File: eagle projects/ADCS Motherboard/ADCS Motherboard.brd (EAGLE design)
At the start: 91 x 91 mm, 142 parts, among them J1 HDR_10_EZFET_DEBUGGER, J11 CNC_3221-10-0300-00, J5 CNC_3221-10-0300-00, J7 TE-1734829-3, Q1 BSR802NL6327HTSA1, Q2 IRLML6246TRPBF, Q3 IRLML2246TRPBF, U1 MSP430F5529IPN, U10 TSV991AILT, U2 TSV991AILT, U3 ADS7841E_2K5, U4 TSV991AILT, U7 HMC1053, U9 BMX160, Y1 32.768kHz, Y2 CSTCR4M00G15L99, Y3 32.768kHz

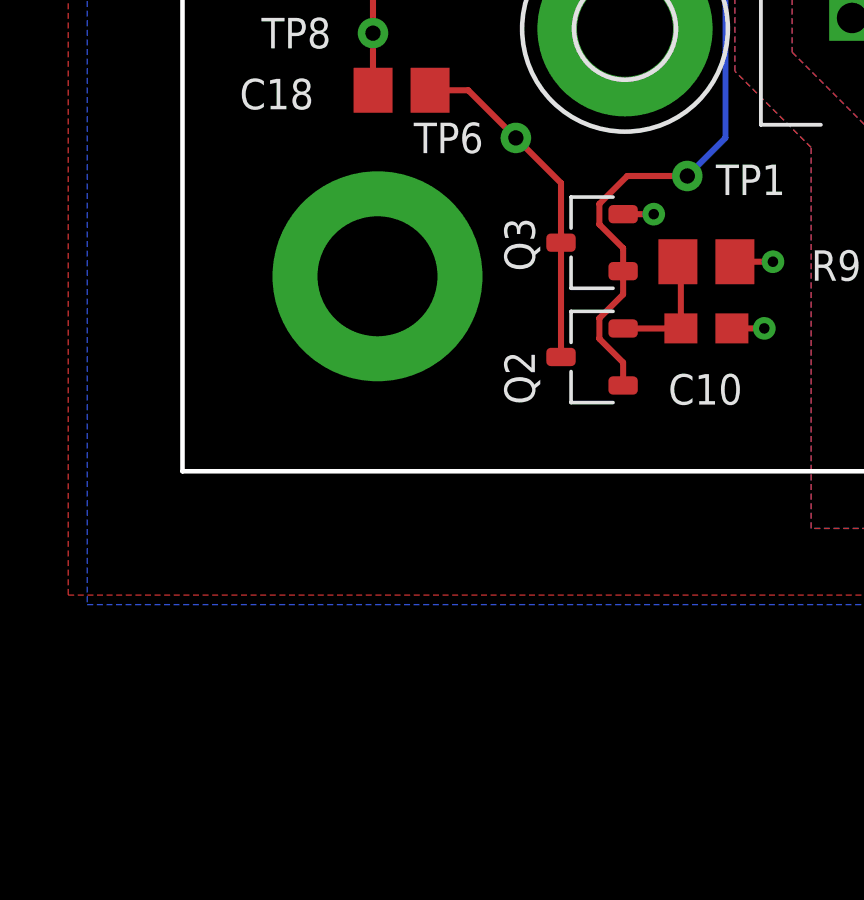
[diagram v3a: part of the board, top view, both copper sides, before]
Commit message: Replace totem pole driver with complementary Mosfets pair package
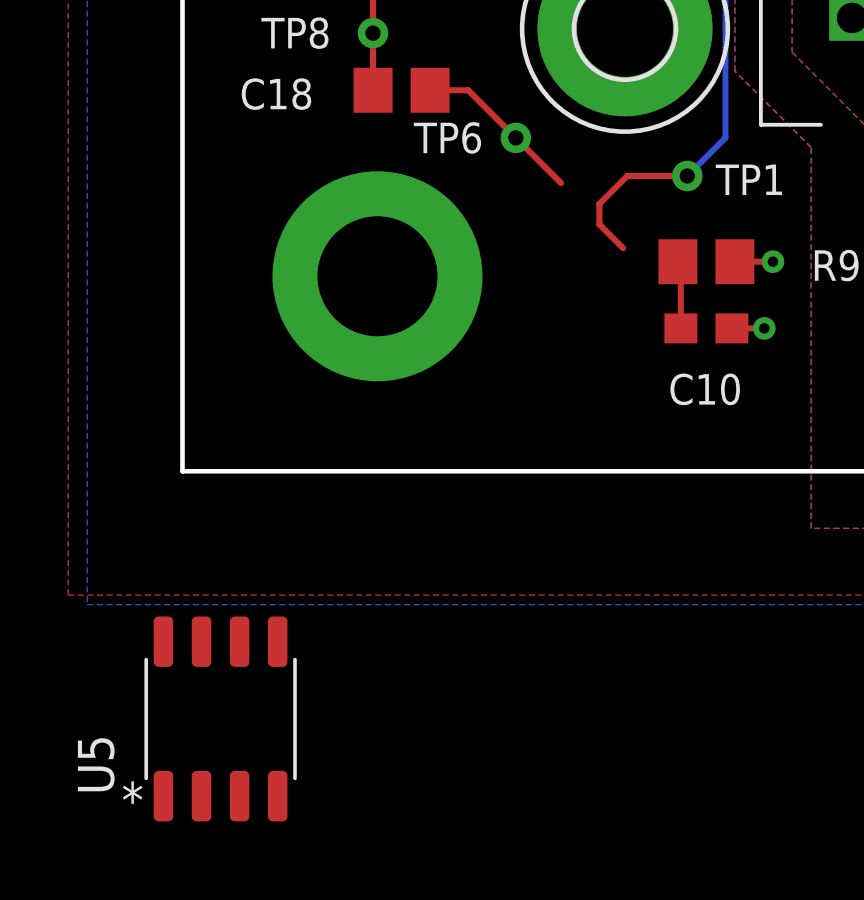
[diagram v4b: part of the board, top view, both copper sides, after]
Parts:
- removed Q2: IRLML6246TRPBF, my_library:SOT23-3P95_237X112L25X40N_MICRO3
- removed Q3: IRLML2246TRPBF, my_library:SOT23-3P95_237X112L25X40N_MICRO3
- added U5: DMC4050SSDQ-13, my_library:SOIC8P127_490X600X175L72X40N_DMC4050SSDQ-13
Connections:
- net GND: now also U5.3; no longer Q3.2
- net HMC1053_RESET: now also U5.2, U5.4; no longer Q2.1, Q3.1
- net N$39: now also U5.1; no longer Q2.2
- net N$9: now also U5.6, U5.7; no longer Q2.3, Q3.3
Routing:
- net N$9: track 11.4 -> 5.65 mm
- net HMC1053_RESET: track 106.7 -> 101.5 mm
- net N$39: track 4.19 -> 2.27 mm
- net GND: track 72.0 -> 71.0 mm, vias 96 -> 95
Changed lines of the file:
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@@
 <attribute name="NAME" x="71.12" y="48.895" size="1.016" layer="25" ratio="10" rot="R180"/>
-</element>
-<element name="Q3" library="my_library" library_urn="urn:adsk.eagle:library:22876504" package="SOT23-3P95_237X112L25X40N_MICRO3" package3d_urn="urn:adsk.eagle:package:24628516/1" value="IRLML2246TRPBF" x="13.6525" y="7.62" smashed="yes" rot="R90">
-<attribute name="NAME" x="11.7475" y="6.6675" size="1.016" layer="25" ratio="10" rot="R90"/>
-</element>
-<element name="Q2" library="my_library" library_urn="urn:adsk.eagle:library:22876504" package="SOT23-3P95_237X112L25X40N_MICRO3" package3d_urn="urn:adsk.eagle:package:24628516/1" value="IRLML6246TRPBF" x="13.6525" y="3.81" smashed="yes" rot="R90">
-<attribute name="NAME" x="11.7475" y="2.2225" size="1.016" layer="25" ratio="10" rot="R90"/>
 </element>
 <element name="J4" library="my_library" library_urn="urn:adsk.eagle:library:22876504" package="1X02" package3d_urn="urn:adsk.eagle:package:24527019/1" value="" x="15.875" y="62.23" smashed="yes">
@@
 <attribute name="POPULARITY" value="35" x="84.455" y="68.2625" size="1.778" layer="27" rot="R90" display="off"/>
 <attribute name="VALUE" x="88.9" y="61.9125" size="1.27" layer="27" rot="R90"/>
+</element>
+<element name="U5" library="my_library" library_urn="urn:adsk.eagle:library:22876504" package="SOIC8P127_490X600X175L72X40N_DMC4050SSDQ-13" value="DMC4050SSDQ-13" x="1.27" y="-8.255" smashed="yes">
+<attribute name="NAME" x="-2.286" y="-10.795" size="1.2" layer="25" font="vector" ratio="10" rot="R90"/>
 </element>
 </elements>
@@
 <contactref element="R36" pad="1"/>
 <contactref element="Q1" pad="2"/>
-<contactref element="Q3" pad="2"/>
-<wire x1="14.6875" y1="8.57" x2="15.7081" y2="8.57" width="0.2032" layer="1"/>
-<via x="15.7081" y="8.57" extent="1-16" drill="0.35"/>
 <wire x1="66.0631" y1="23.226" x2="66.0146" y2="23.1775" width="0.2032" layer="1"/>
 <wire x1="72.175" y1="51.7525" x2="71.0944" y2="51.7525" width="0.2032" layer="1"/>
@@
 <wire x1="83.955" y1="36.195" x2="83.0744" y2="36.195" width="0.2032" layer="1"/>
 <via x="83.0744" y="36.195" extent="1-16" drill="0.35"/>
+<contactref element="U5" pad="3"/>
 <wire x1="66.0631" y1="24.1681" x2="66.03960625" y2="24.130009375" width="0" layer="19" extent="1-1"/>
+<wire x1="1.905" y1="-10.83" x2="18.3125" y2="4.7625" width="0" layer="19" extent="1-1"/>
 </signal>
 <signal name="TARGET_PUR">
@@
 <signal name="HMC1053_RESET">
 <contactref element="TP1" pad="1"/>
-<contactref element="Q3" pad="1"/>
-<contactref element="Q2" pad="1"/>
 <via x="34.925" y="49.53" extent="1-16" drill="0.35"/>
 <wire x1="13.8959" y1="8.91238125" x2="13.8959" y2="8.22761875" width="0.2032" layer="1"/>
@@
 <wire x1="14.82601875" y1="9.8425" x2="13.8959" y2="8.91238125" width="0.2032" layer="1"/>
 <wire x1="13.8959" y1="8.22761875" x2="14.6875" y2="7.43601875" width="0.2032" layer="1"/>
-<wire x1="14.6875" y1="7.43601875" x2="14.6875" y2="6.67" width="0.2032" layer="1"/>
 <contactref element="U1" pad="2"/>
 <wire x1="68.023025" y1="49.8602" x2="38.19795" y2="49.8602" width="0.2032" layer="1"/>
@@
 <wire x1="29.5275" y1="46.6725" x2="32.0675" y2="46.6725" width="0.2032" layer="16"/>
 <wire x1="32.0675" y1="46.6725" x2="34.925" y2="49.53" width="0.2032" layer="16"/>
-<wire x1="13.8959" y1="5.10238125" x2="13.8959" y2="4.41761875" width="0.2032" layer="1"/>
-<wire x1="14.6875" y1="6.67" x2="14.6875" y2="5.89398125" width="0.2032" layer="1"/>
-<wire x1="14.6875" y1="3.62601875" x2="14.6875" y2="2.86" width="0.2032" layer="1"/>
-<wire x1="14.6875" y1="5.89398125" x2="13.8959" y2="5.10238125" width="0.2032" layer="1"/>
-<wire x1="13.8959" y1="4.41761875" x2="14.6875" y2="3.62601875" width="0.2032" layer="1"/>
 <wire x1="18.0975" y1="36.5125" x2="18.0975" y2="11.1125" width="0.2032" layer="16"/>
 <wire x1="18.0975" y1="11.1125" x2="16.8275" y2="9.8425" width="0.2032" layer="16"/>
@@
 <wire x1="71.56" y1="41.308025" x2="69.644" y2="43.224025" width="0.2032" layer="1"/>
 <wire x1="69.644" y1="48.239225" x2="68.023025" y2="49.8602" width="0.2032" layer="1"/>
+<contactref element="U5" pad="4"/>
+<contactref element="U5" pad="2"/>
+<wire x1="3.175" y1="-10.83" x2="14.6875" y2="7.43601875" width="0" layer="19" extent="1-1"/>
+<wire x1="0.635" y1="-10.83" x2="3.175" y2="-10.83" width="0" layer="19" extent="1-1"/>
 </signal>
 <signal name="N$39">
 <contactref element="C10" pad="2"/>
 <contactref element="R9" pad="1"/>
-<contactref element="Q2" pad="2"/>
 <wire x1="16.6125" y1="4.7625" x2="16.61" y2="4.76" width="0.2032" layer="1"/>
-<wire x1="16.61" y1="4.76" x2="14.6875" y2="4.76" width="0.2032" layer="1"/>
 <wire x1="16.5125" y1="6.985" x2="16.6125" y2="6.885" width="0.2032" layer="1"/>
 <wire x1="16.6125" y1="6.885" x2="16.6125" y2="4.7625" width="0.2032" layer="1"/>
+<contactref element="U5" pad="1"/>
+<wire x1="-0.635" y1="-10.83" x2="16.6125" y2="4.7625" width="0" layer="19" extent="1-1"/>
 </signal>
 <signal name="OUT_B_P" class="1">
@@
 <signal name="N$9">
 <contactref element="C18" pad="1"/>
-<wire x1="12.6175" y1="3.81" x2="12.6175" y2="7.62" width="0.2032" layer="1"/>
-<contactref element="Q3" pad="3"/>
-<contactref element="Q2" pad="3"/>
 <contactref element="TP6" pad="1"/>
 <wire x1="8.2525" y1="12.7" x2="9.525" y2="12.7" width="0.2032" layer="1"/>
 <wire x1="11.1125" y1="11.1125" x2="9.525" y2="12.7" width="0.2032" layer="1"/>
 <wire x1="11.1125" y1="11.1125" x2="12.6175" y2="9.6075" width="0.2032" layer="1"/>
-<wire x1="12.6175" y1="9.6075" x2="12.6175" y2="7.62" width="0.2032" layer="1"/>
+<contactref element="U5" pad="7"/>
+<contactref element="U5" pad="6"/>
+<wire x1="1.905" y1="-5.68" x2="12.6175" y2="9.6075" width="0" layer="19" extent="1-1"/>
+<wire x1="0.635" y1="-5.68" x2="1.905" y2="-5.68" width="0" layer="19" extent="1-1"/>
 </signal>
 <signal name="UCB1_I2C_SCL">

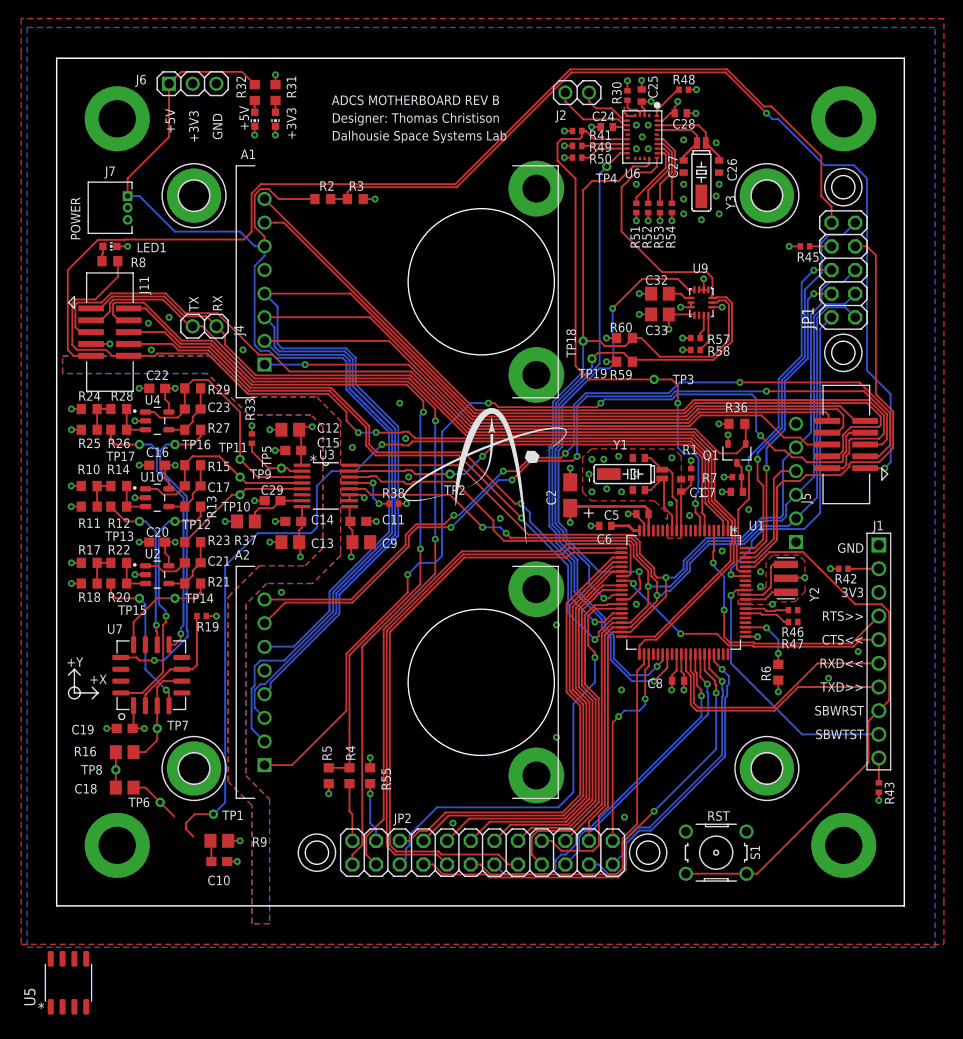
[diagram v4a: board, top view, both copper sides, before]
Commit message: Added new mosfet pair to layout
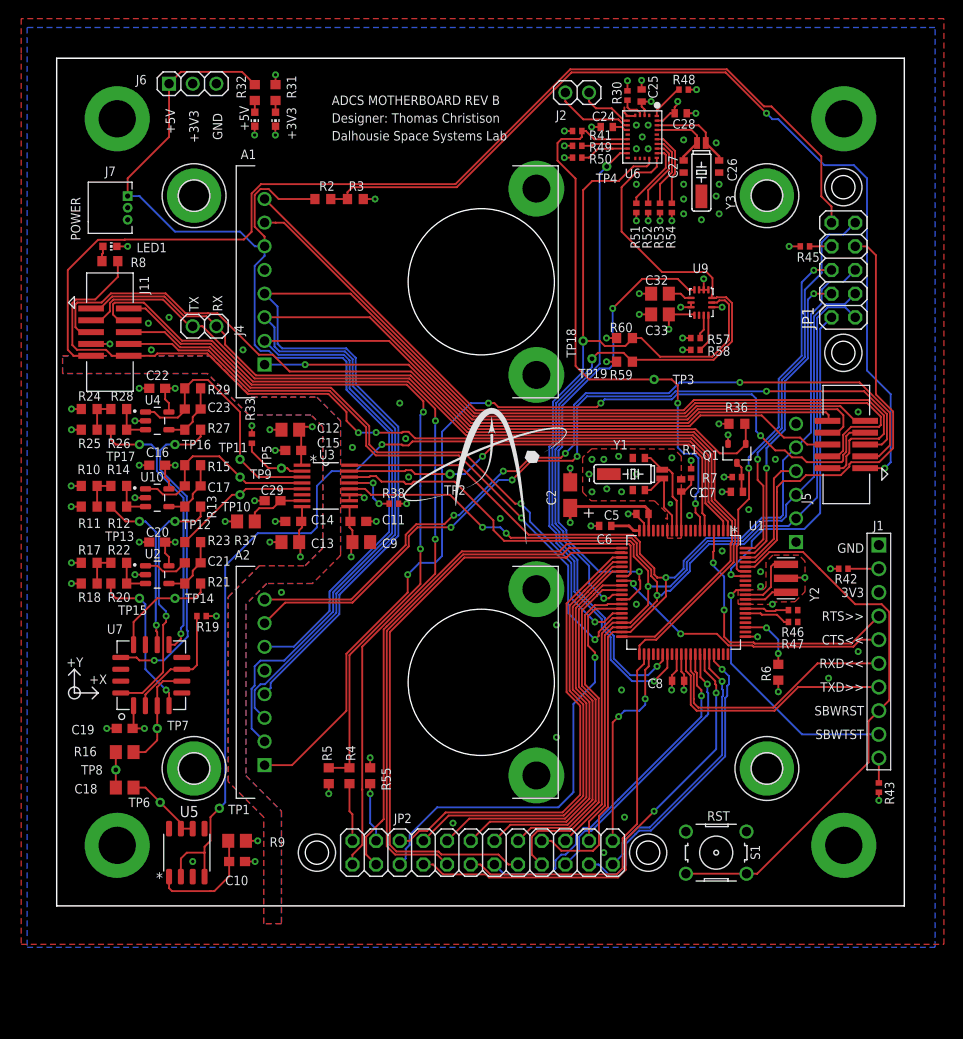
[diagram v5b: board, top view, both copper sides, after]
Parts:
- moved U5 18.9 mm to (14.0, 5.71)
- moved C10 1.91 mm to (19.4, 4.76)
- moved R9 1.91 mm to (19.4, 6.99)
- moved TP1 0.90 mm to (17.5, 10.5)
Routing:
- net N$39: track 2.27 -> 12.3 mm
- net HMC1053_RESET: track 101.5 -> 108.2 mm
- net N$9: track 5.65 -> 8.53 mm
- net GND: vias 95 -> 99

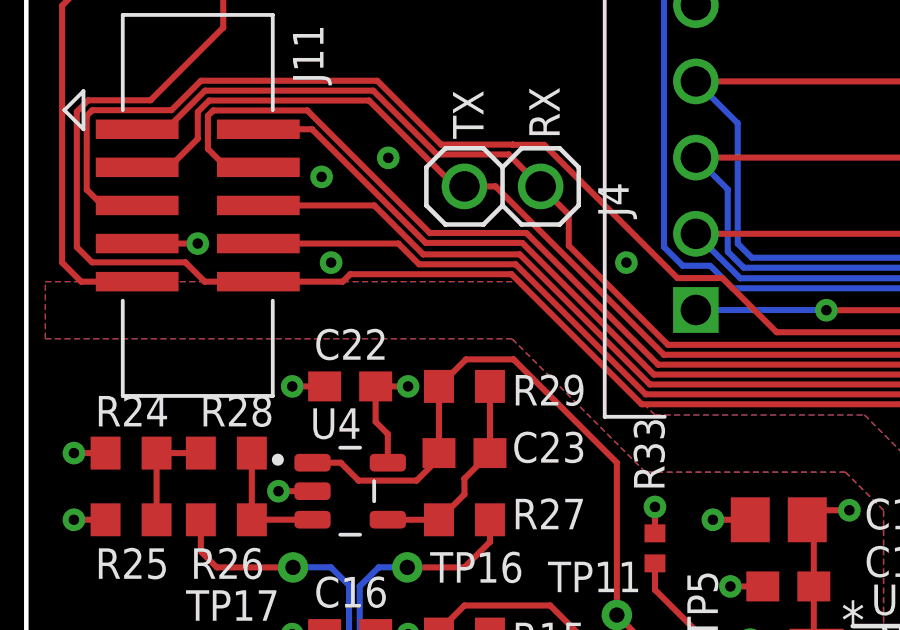
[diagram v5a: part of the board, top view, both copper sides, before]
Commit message: Grounded standoff mounting hole pins
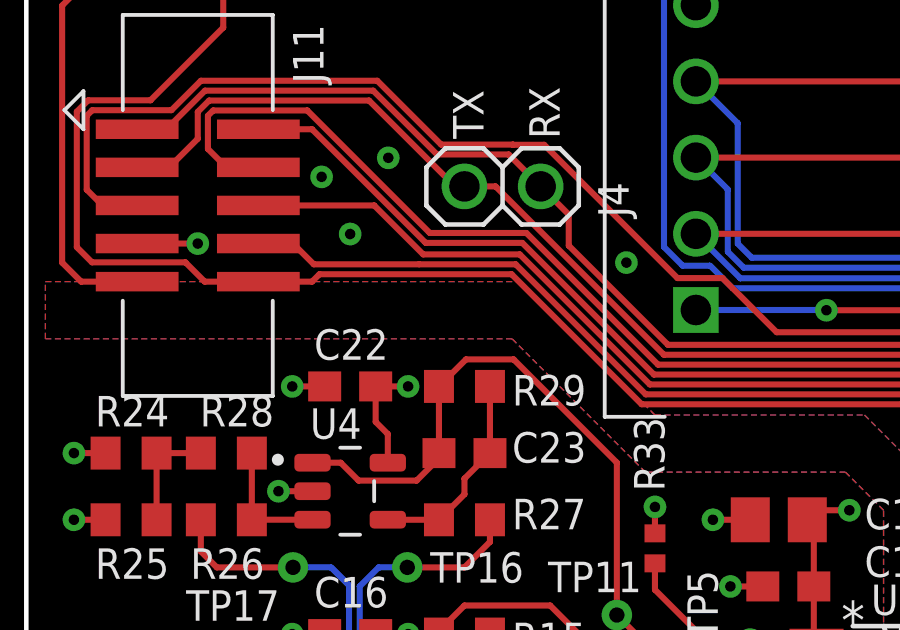
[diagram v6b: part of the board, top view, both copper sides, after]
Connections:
- net GND: now also H1.B3,2, H2.B3,2, H3.B3,2, H4.B3,2
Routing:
- net MSP430_ACTIVE: track 95.3 -> 94.8 mm
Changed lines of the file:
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@@
 <setting verticaltext="up"/>
 </settings>
-<grid distance="25" unitdist="mil" unit="mil" style="lines" multiple="1" display="yes" altdistance="12.5" altunitdist="mil" altunit="mil"/>
+<grid distance="25" unitdist="mil" unit="mm" style="lines" multiple="1" display="yes" altdistance="12.5" altunitdist="mil" altunit="mil"/>
 <layers>
 <layer number="1" name="Top" color="4" fill="1" visible="yes" active="yes"/>
@@
 <via x="9.8425" y="62.5475" extent="1-16" drill="0.35"/>
 <via x="20.0025" y="59.69" extent="1-16" drill="0.35"/>
-<via x="10.16" y="59.69" extent="1-16" drill="0.35"/>
 <via x="47.625" y="41.5925" extent="1-16" drill="0.35"/>
 <via x="67.945" y="41.91" extent="1-16" drill="0.35"/>
@@
 <via x="77.1525" y="47.9425" extent="1-16" drill="0.35"/>
 <via x="86.0425" y="53.0225" extent="1-16" drill="0.35"/>
+<contactref element="H1" pad="B3,2"/>
+<contactref element="H2" pad="B3,2"/>
+<contactref element="H3" pad="B3,2"/>
+<contactref element="H4" pad="B3,2"/>
+<via x="10.795" y="60.6425" extent="1-16" drill="0.35"/>
 <wire x1="66.0631" y1="24.1681" x2="66.03960625" y2="24.130009375" width="0" layer="19" extent="1-1"/>
 </signal>
@@
 <wire x1="29.16979375" y1="54.96770625" x2="31.115" y2="53.0225" width="0.2032" layer="1"/>
 <wire x1="20.51059375" y1="54.96770625" x2="29.16979375" y2="54.96770625" width="0.2032" layer="1"/>
-<wire x1="16.17583125" y1="59.30246875" x2="10.795" y2="59.30246875" width="0.2032" layer="1"/>
-<wire x1="16.17583125" y1="59.30246875" x2="20.51059375" y2="54.96770625" width="0.2032" layer="1"/>
-<wire x1="10.795" y1="59.30246875" x2="10.54753125" y2="59.055" width="0.2032" layer="1"/>
-<wire x1="10.54753125" y1="59.055" x2="7.735" y2="59.055" width="0.2032" layer="1"/>
+<wire x1="20.51059375" y1="54.96770625" x2="16.17583125" y2="59.30246875" width="0.2032" layer="1"/>
 <wire x1="37.76895" y1="50.8988" x2="37.16105" y2="50.8988" width="0.2032" layer="1"/>
 <wire x1="37.16105" y1="50.8988" x2="37.06225" y2="50.8" width="0.2032" layer="1"/>
@@
 <wire x1="72.06" y1="41.275" x2="69.9742" y2="43.3608" width="0.2032" layer="1"/>
 <wire x1="69.9742" y1="48.376" x2="68.1598" y2="50.1904" width="0.2032" layer="1"/>
+<wire x1="9.77246875" y1="59.30246875" x2="9.525" y2="59.055" width="0.2032" layer="1"/>
+<wire x1="9.525" y1="59.055" x2="8.255" y2="59.055" width="0.2032" layer="1"/>
+<wire x1="16.17583125" y1="59.30246875" x2="9.77246875" y2="59.30246875" width="0.2032" layer="1"/>
+<wire x1="7.735" y1="59.055" x2="8.255" y2="59.055" width="0" layer="19" extent="1-1"/>
 </signal>
 <signal name="RESERVED_1">
@@
 <wire x1="29.30656875" y1="55.29790625" x2="33.226" y2="51.378475" width="0.2032" layer="1"/>
 <wire x1="29.30656875" y1="55.29790625" x2="20.64736875" y2="55.29790625" width="0.2032" layer="1"/>
-<wire x1="12.40105" y1="60.325" x2="7.735" y2="60.325" width="0.2032" layer="1"/>
+<wire x1="8.89" y1="60.325" x2="7.735" y2="60.325" width="0.2032" layer="1"/>
 <wire x1="16.31260625" y1="59.63266875" x2="13.09338125" y2="59.63266875" width="0.2032" layer="1"/>
 <wire x1="20.64736875" y1="55.29790625" x2="16.31260625" y2="59.63266875" width="0.2032" layer="1"/>
-<wire x1="13.09338125" y1="59.63266875" x2="12.40105" y2="60.325" width="0.2032" layer="1"/>
 <wire x1="43.18715" y1="48.35665" x2="34.262575" y2="48.35665" width="0.2032" layer="1"/>
 <wire x1="49.8994" y1="41.6444" x2="43.18715" y2="48.35665" width="0.2032" layer="1"/>
 <wire x1="34.262575" y1="48.35665" x2="33.226" y2="49.393225" width="0.2032" layer="1"/>
+<wire x1="13.09338125" y1="59.63266875" x2="9.58233125" y2="59.63266875" width="0.2032" layer="1"/>
+<wire x1="9.58233125" y1="59.63266875" x2="8.89" y2="60.325" width="0.2032" layer="1"/>
 </signal>
 <signal name="RW_Y_SPEED_CTRL">
